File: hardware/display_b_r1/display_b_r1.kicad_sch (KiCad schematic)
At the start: 20 parts

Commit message: Display board layout is now 95% complete, the number of caps on the board might need some further tweaking and there are also some gaps where a few more LEDs could fit. Additionally I've decided to provide the option to use the hinges as the ground connection allowing more +5V channels on the FFC connectors which should mean more current carrying capacity. The new power board schematic has had some changes, namely the vreg has changed and so have some of the passives around it, more input protect has been added, a MOV for over voltage protection and an NMOS for reverse pol. Looking at the new vreg the power dissipation before it cooks itself (~1.1W) isn't great but it's enough for about 2.5A (at around 93% eff.) for the LEDs which hasn't usually been the bottleneck (looking at you 9V batteries). This means we're expecting around 1.8A peak input current at a Vin of 7V and need to size the fuze around that as much more current and the vreg is cooked. Might look into a over voltage shutout circuit if it seems like we're blowing fuses too often.
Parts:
- removed J?: 8-pin FPC Connector, symbol Connector_Generic:Conn_01x08
- added C109, C110, C111, C112, C113, C114, C115, C116, C117, C118, C119, C120, C121, C122, C123, C124, C125, C126, C127, C129, C130, C131, C132, C133, C134, C135, C136, C137, C138, C139, C140, C141, C142, C143, C144, C145, C146, C147: 22u 10V, Capacitor_SMD:C_0603_1608Metric, symbol Device:C_Small
- added D101, D102, D103, D104, D107, D108, D109, D110, D111, D112, D113, D114, D115, D116, D117, D118, D119, D120, D121, D122, D123, D124, D125, D126, D127, D128, D129, D130, D131, D132, D133, D134, D135, D136, D137, D138, D139, D140, D142, D143, D144, D145, D146, D147, D148, D149, D151, D152, D153, D154, D155, D156, D157, D158, D160, D161, D162, D163, D164, D165, D166, D167, D169, D170, D172, D173, D174, D175, D176, D178, D179, D180, D182, D183, D185, D188, D189, D191, D192, D193, D194, D196, D197, D199, D200, D202, D204, D205, D206, D207, D208, D209, D210, D212, D213, D214, D215, D216, D217, D218, D220, D221, D222, D223, D224, D225, D226, D229, D230, D231, D232, D233, D234, D235, D238, D239, D240, D241, D242, D243, D244, D247, D248, D249, D250, D251, D252, D253, D256, D257, D258, D259, D260, D261, D262, D265, D266, D267, D270, D271: APA102-2020, rave_shades:LED-APA102-2020, symbol LED:APA102-2020
- added H101, H102, H103, H104: MountingHole_Pad, rave_shades:M1.4 Mounting Hole, symbol Mechanical:MountingHole_Pad
- added J102: Conn_01x08, rave_shades:CF35082D0RE-NH, symbol rave_shades:Conn_01x08
- added JP101, JP102: SolderJumper_3_Open, Jumper:SolderJumper-3_P1.3mm_Open_Pad1.0x1.5mm, symbol Jumper:SolderJumper_3_Open
- C101, C102, C103, C104, C105, C106, C107, C108: renamed from C?; footprint (none) -> Capacitor_SMD:C_0603_1608Metric
- D187, D195, D203, D211, D219, D228, D237, D246, D255, D264: renamed from D?; footprint LED_SMD:LED-APA102-2020 -> rave_shades:LED-APA102-2020
- J101: renamed from J?; footprint (none) -> rave_shades:CF35082D0RE-NH; symbol Connector_Generic:Conn_01x08 -> rave_shades:Conn_01x08
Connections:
- net +5V: now also C109.1, C110.1, C111.1, C112.1, C113.1, C114.1, C115.1, C116.1, C117.1, C118.1, C119.1, C120.1, C121.1, C122.1, C123.1, C124.1, C125.1, C126.1, C127.1, C129.1, C130.1, C131.1, C132.1, C133.1, C134.1, C135.1, C136.1, C137.1, C138.1, C139.1, C140.1, C141.1, C142.1, C143.1, C144.1, C145.1, C146.1, C147.1, D101.1 (VDD), D102.1 (VDD), D103.1 (VDD), D104.1 (VDD), D107.1 (VDD), D108.1 (VDD), D109.1 (VDD), D110.1 (VDD), D111.1 (VDD), D112.1 (VDD), D113.1 (VDD), D114.1 (VDD), D115.1 (VDD), D116.1 (VDD), D117.1 (VDD), D118.1 (VDD), D119.1 (VDD), D120.1 (VDD), D121.1 (VDD), D122.1 (VDD), D123.1 (VDD), D124.1 (VDD), D125.1 (VDD), D126.1 (VDD), D127.1 (VDD), D128.1 (VDD), D129.1 (VDD), D130.1 (VDD), D131.1 (VDD), D132.1 (VDD), D133.1 (VDD), D134.1 (VDD), D135.1 (VDD), D136.1 (VDD), D137.1 (VDD), D138.1 (VDD), D139.1 (VDD), D140.1 (VDD), D142.1 (VDD), D143.1 (VDD), D144.1 (VDD), D145.1 (VDD), D146.1 (VDD), D147.1 (VDD), D148.1 (VDD), D149.1 (VDD), D151.1 (VDD), D152.1 (VDD), D153.1 (VDD), D154.1 (VDD), D155.1 (VDD), D156.1 (VDD), D157.1 (VDD), D158.1 (VDD), D160.1 (VDD), D161.1 (VDD), D162.1 (VDD), D163.1 (VDD), D164.1 (VDD), D165.1 (VDD), D166.1 (VDD), D167.1 (VDD), D169.1 (VDD), D170.1 (VDD), D172.1 (VDD), D173.1 (VDD), D174.1 (VDD), D175.1 (VDD), D176.1 (VDD), D178.1 (VDD), D179.1 (VDD), D180.1 (VDD), D182.1 (VDD), D183.1 (VDD), D185.1 (VDD), D188.1 (VDD), D189.1 (VDD), D191.1 (VDD), D192.1 (VDD), D193.1 (VDD), D194.1 (VDD), D196.1 (VDD), D197.1 (VDD), D199.1 (VDD), D200.1 (VDD), D202.1 (VDD), D204.1 (VDD), D205.1 (VDD), D206.1 (VDD), D207.1 (VDD), D208.1 (VDD), D209.1 (VDD), D210.1 (VDD), D212.1 (VDD), D213.1 (VDD), D214.1 (VDD), D215.1 (VDD), D216.1 (VDD), D217.1 (VDD), D218.1 (VDD), D220.1 (VDD), D221.1 (VDD), D222.1 (VDD), D223.1 (VDD), D224.1 (VDD), D225.1 (VDD), D226.1 (VDD), D229.1 (VDD), D230.1 (VDD), D231.1 (VDD), D232.1 (VDD), D233.1 (VDD), D234.1 (VDD), D235.1 (VDD), D238.1 (VDD), D239.1 (VDD), D240.1 (VDD), D241.1 (VDD), D242.1 (VDD), D243.1 (VDD), D244.1 (VDD), D247.1 (VDD), D248.1 (VDD), D249.1 (VDD), D250.1 (VDD), D251.1 (VDD), D252.1 (VDD), D253.1 (VDD), D256.1 (VDD), D257.1 (VDD), D258.1 (VDD), D259.1 (VDD), D260.1 (VDD), D261.1 (VDD), D262.1 (VDD), D265.1 (VDD), D266.1 (VDD), D267.1 (VDD), D270.1 (VDD), D271.1 (VDD), J102.4 (Pin_4), J102.5 (Pin_5), JP101.1 (A), JP102.1 (A)
- net GND: now also J101.9 (NC), C109.2, C110.2, C111.2, C112.2, C113.2, C114.2, C115.2, C116.2, C117.2, C118.2, C119.2, C120.2, C121.2, C122.2, C123.2, C124.2, C125.2, C126.2, C127.2, C129.2, C130.2, C131.2, C132.2, C133.2, C134.2, C135.2, C136.2, C137.2, C138.2, C139.2, C140.2, C141.2, C142.2, C143.2, C144.2, C145.2, C146.2, C147.2, D101.6 (GND), D102.6 (GND), D103.6 (GND), D104.6 (GND), D107.6 (GND), D108.6 (GND), D109.6 (GND), D110.6 (GND), D111.6 (GND), D112.6 (GND), D113.6 (GND), D114.6 (GND), D115.6 (GND), D116.6 (GND), D117.6 (GND), D118.6 (GND), D119.6 (GND), D120.6 (GND), D121.6 (GND), D122.6 (GND), D123.6 (GND), D124.6 (GND), D125.6 (GND), D126.6 (GND), D127.6 (GND), D128.6 (GND), D129.6 (GND), D130.6 (GND), D131.6 (GND), D132.6 (GND), D133.6 (GND), D134.6 (GND), D135.6 (GND), D136.6 (GND), D137.6 (GND), D138.6 (GND), D139.6 (GND), D140.6 (GND), D142.6 (GND), D143.6 (GND), D144.6 (GND), D145.6 (GND), D146.6 (GND), D147.6 (GND), D148.6 (GND), D149.6 (GND), D151.6 (GND), D152.6 (GND), D153.6 (GND), D154.6 (GND), D155.6 (GND), D156.6 (GND), D157.6 (GND), D158.6 (GND), D160.6 (GND), D161.6 (GND), D162.6 (GND), D163.6 (GND), D164.6 (GND), D165.6 (GND), D166.6 (GND), D167.6 (GND), D169.6 (GND), D170.6 (GND), D172.6 (GND), D173.6 (GND), D174.6 (GND), D175.6 (GND), D176.6 (GND), D178.6 (GND), D179.6 (GND), D180.6 (GND), D182.6 (GND), D183.6 (GND), D185.6 (GND), D188.6 (GND), D189.6 (GND), D191.6 (GND), D192.6 (GND), D193.6 (GND), D194.6 (GND), D196.6 (GND), D197.6 (GND), D199.6 (GND), D200.6 (GND), D202.6 (GND), D204.6 (GND), D205.6 (GND), D206.6 (GND), D207.6 (GND), D208.6 (GND), D209.6 (GND), D210.6 (GND), D212.6 (GND), D213.6 (GND), D214.6 (GND), D215.6 (GND), D216.6 (GND), D217.6 (GND), D218.6 (GND), D220.6 (GND), D221.6 (GND), D222.6 (GND), D223.6 (GND), D224.6 (GND), D225.6 (GND), D226.6 (GND), D229.6 (GND), D230.6 (GND), D231.6 (GND), D232.6 (GND), D233.6 (GND), D234.6 (GND), D235.6 (GND), D238.6 (GND), D239.6 (GND), D240.6 (GND), D241.6 (GND), D242.6 (GND), D243.6 (GND), D244.6 (GND), D247.6 (GND), D248.6 (GND), D249.6 (GND), D250.6 (GND), D251.6 (GND), D252.6 (GND), D253.6 (GND), D256.6 (GND), D257.6 (GND), D258.6 (GND), D259.6 (GND), D260.6 (GND), D261.6 (GND), D262.6 (GND), D265.6 (GND), D266.6 (GND), D267.6 (GND), D270.6 (GND), D271.6 (GND), H101.1, H102.1, H103.1, H104.1, J102.9 (NC), JP101.3 (B), JP102.3 (B); no longer J101.1 (Pin_1), J101.3 (Pin_3), J101.6 (Pin_6)
- net LED_CLK_5V0: now also J102.7 (Pin_7)
- net LED_MOSI_5V0: now also J102.8 (Pin_8)
- net SPARE_0_5V0: now also J102.2 (Pin_2)
- net SPARE_1_5V0: now also J102.1 (Pin_1)
- net at D187.2 (CKO): now also D188.5 (CKI)
- net at D187.3 (SDO): now also D188.4 (SDI)
- new net: D143.2 (CKO), D152.5 (CKI)
- new net: D143.3 (SDO), D152.4 (SDI)
- new net: D134.3 (SDO), D143.4 (SDI)
- new net: D134.2 (CKO), D143.5 (CKI)
- new net: D196.2 (CKO), D204.5 (CKI)
- new net: D196.3 (SDO), D204.4 (SDI)
- new net: D188.3 (SDO), D196.4 (SDI)
- new net: D188.2 (CKO), D196.5 (CKI)
- new net: D176.2 (CKO), D185.5 (CKI)
- new net: D176.3 (SDO), D185.4 (SDI)
- new net: D167.3 (SDO), D176.4 (SDI)
- new net: D167.2 (CKO), D176.5 (CKI)
- new net: D153.5 (CKI), D162.2 (CKO)
- new net: D153.4 (SDI), D162.3 (SDO)
- new net: D162.4 (SDI), D180.3 (SDO)
- new net: D162.5 (CKI), D180.2 (CKO)
- new net: D102.2 (CKO), D110.5 (CKI)
- new net: D102.3 (SDO), D110.4 (SDI)
- new net: D101.3 (SDO), D102.4 (SDI)
- new net: D101.2 (CKO), D102.5 (CKI)
- new net: D215.5 (CKI), D223.2 (CKO)
- new net: D215.4 (SDI), D223.3 (SDO)
- new net: D223.4 (SDI), D232.3 (SDO)
- new net: D223.5 (CKI), D232.2 (CKO)
- new net: D191.2 (CKO), D192.5 (CKI)
- new net: D191.3 (SDO), D192.4 (SDI)
- new net: D191.4 (SDI), D199.3 (SDO)
- new net: D191.5 (CKI), D199.2 (CKO)
- new net: D104.2 (CKO), D112.5 (CKI)
- new net: D104.3 (SDO), D112.4 (SDI)
- new net: D103.3 (SDO), D104.4 (SDI)
- new net: D103.2 (CKO), D104.5 (CKI)
- new net: D214.2 (CKO), D222.5 (CKI)
- new net: D214.3 (SDO), D222.4 (SDI)
- new net: D206.3 (SDO), D214.4 (SDI)
- new net: D206.2 (CKO), D214.5 (CKI)
- new net: D213.5 (CKI), D221.2 (CKO)
- new net: D213.4 (SDI), D221.3 (SDO)
- new net: D221.4 (SDI), D230.3 (SDO)
- new net: D221.5 (CKI), D230.2 (CKO)
- new net: D122.2 (CKO), D130.5 (CKI)
- new net: D122.3 (SDO), D130.4 (SDI)
- new net: D114.3 (SDO), D122.4 (SDI)
- new net: D114.2 (CKO), D122.5 (CKI)
- new net: D173.5 (CKI), D182.2 (CKO)
- new net: D173.4 (SDI), D182.3 (SDO)
- new net: D172.3 (SDO), D182.4 (SDI)
- new net: D172.2 (CKO), D182.5 (CKI)
- new net: D192.2 (CKO), D200.5 (CKI)
- new net: D192.3 (SDO), D200.4 (SDI)
- new net: D222.2 (CKO), D231.5 (CKI)
- new net: D222.3 (SDO), D231.4 (SDI)
- new net: D234.5 (CKI), D243.2 (CKO)
- new net: D234.4 (SDI), D243.3 (SDO)
- new net: D243.4 (SDI), D252.3 (SDO)
- new net: D243.5 (CKI), D252.2 (CKO)
- new net: D156.2 (CKO), D165.5 (CKI)
- new net: D156.3 (SDO), D165.4 (SDI)
- new net: D147.3 (SDO), D156.4 (SDI)
- new net: D147.2 (CKO), D156.5 (CKI)
- new net: D178.5 (CKI), D271.2 (CKO)
- new net: D178.4 (SDI), D271.3 (SDO)
- new net: D262.3 (SDO), D271.4 (SDI)
- new net: D262.2 (CKO), D271.5 (CKI)
- new net: D265.2 (CKO), D266.5 (CKI)
- new net: D265.3 (SDO), D266.4 (SDI)
- new net: D256.3 (SDO), D265.4 (SDI)
- new net: D256.2 (CKO), D265.5 (CKI)
- new net: D148.5 (CKI), D157.2 (CKO)
- new net: D148.4 (SDI), D157.3 (SDO)
- new net: D157.4 (SDI), D166.3 (SDO)
- new net: D157.5 (CKI), D166.2 (CKO)
- new net: D149.2 (CKO), D158.5 (CKI)
- new net: D149.3 (SDO), D158.4 (SDI)
- new net: D140.3 (SDO), D149.4 (SDI)
- new net: D140.2 (CKO), D149.5 (CKI)
- new net: D199.4 (SDI), D207.3 (SDO)
- new net: D199.5 (CKI), D207.2 (CKO)
- new net: D241.5 (CKI), D250.2 (CKO)
- new net: D241.4 (SDI), D250.3 (SDO)
- new net: D250.4 (SDI), D259.3 (SDO)
- new net: D250.5 (CKI), D259.2 (CKO)
- new net: D107.2 (CKO), D108.5 (CKI)
- new net: D107.3 (SDO), D108.4 (SDI)
- new net: D107.4 (SDI), D115.3 (SDO)
- new net: D107.5 (CKI), D115.2 (CKO)
- new net: D212.2 (CKO), D220.5 (CKI)
- new net: D212.3 (SDO), D220.4 (SDI)
- new net: D204.3 (SDO), D212.4 (SDI)
- new net: D204.2 (CKO), D212.5 (CKI)
- new net: D235.2 (CKO), D244.5 (CKI)
- new net: D235.3 (SDO), D244.4 (SDI)
- new net: D226.3 (SDO), D235.4 (SDI)
- new net: D226.2 (CKO), D235.5 (CKI)
- new net: D138.3 (SDO), D147.4 (SDI)
- new net: D138.2 (CKO), D147.5 (CKI)
- new net: D189.3 (SDO), D206.4 (SDI)
- new net: D189.2 (CKO), D206.5 (CKI)
- new net: D233.2 (CKO), D242.5 (CKI)
- new net: D233.3 (SDO), D242.4 (SDI)
- new net: D224.3 (SDO), D233.4 (SDI)
- new net: D224.2 (CKO), D233.5 (CKI)
- new net: D179.3 (SDO), D180.4 (SDI)
- new net: D179.2 (CKO), D180.5 (CKI)
- new net: D166.5 (CKI), D175.2 (CKO)
- new net: D166.4 (SDI), D175.3 (SDO)
- new net: D175.4 (SDI), D183.3 (SDO)
- new net: D175.5 (CKI), D183.2 (CKO)
- new net: D144.5 (CKI), D153.2 (CKO)
- new net: D144.4 (SDI), D153.3 (SDO)
- new net: D103.4 (SDI), D111.3 (SDO)
- new net: D103.5 (CKI), D111.2 (CKO)
- new net: D129.5 (CKI), D137.2 (CKO)
- new net: D129.4 (SDI), D137.3 (SDO)
- new net: D137.4 (SDI), D146.3 (SDO)
- new net: D137.5 (CKI), D146.2 (CKO)
- new net: D232.4 (SDI), D241.3 (SDO)
- new net: D232.5 (CKI), D241.2 (CKO)
- new net: D230.5 (CKI), D239.2 (CKO)
- new net: D230.4 (SDI), D239.3 (SDO)
- new net: D239.4 (SDI), D248.3 (SDO)
- new net: D239.5 (CKI), D248.2 (CKO)
- new net: D240.2 (CKO), D249.5 (CKI)
- new net: D240.3 (SDO), D249.4 (SDI)
- new net: D231.3 (SDO), D240.4 (SDI)
- new net: D231.2 (CKO), D240.5 (CKI)
- new net: D151.5 (CKI), D160.2 (CKO)
- new net: D151.4 (SDI), D160.3 (SDO)
- new net: D160.4 (SDI), D169.3 (SDO)
- new net: D160.5 (CKI), D169.2 (CKO)
- new net: D128.2 (CKO), D136.5 (CKI)
- new net: D128.3 (SDO), D136.4 (SDI)
- new net: D120.3 (SDO), D128.4 (SDI)
- new net: D120.2 (CKO), D128.5 (CKI)
- new net: D101.4 (SDI), D109.3 (SDO)
- new net: D101.5 (CKI), D109.2 (CKO)
- new net: D146.4 (SDI), D155.3 (SDO)
- new net: D146.5 (CKI), D155.2 (CKO)
- new net: D189.4 (SDI), D197.3 (SDO)
- new net: D189.5 (CKI), D197.2 (CKO)
- new net: D123.5 (CKI), D131.2 (CKO)
- new net: D123.4 (SDI), D131.3 (SDO)
- new net: D131.4 (SDI), D139.3 (SDO)
- new net: D131.5 (CKI), D139.2 (CKO)
- new net: D164.5 (CKI), D173.2 (CKO)
- new net: D164.4 (SDI), D173.3 (SDO)
- new net: D109.5 (CKI), D117.2 (CKO)
- new net: D109.4 (SDI), D117.3 (SDO)
- new net: D117.4 (SDI), D125.3 (SDO)
- new net: D117.5 (CKI), D125.2 (CKO)
- new net: D112.3 (SDO), D120.4 (SDI)
- new net: D112.2 (CKO), D120.5 (CKI)
- new net: D125.4 (SDI), D133.3 (SDO)
- new net: D125.5 (CKI), D133.2 (CKO)
- new net: D113.2 (CKO), D114.5 (CKI)
- new net: D113.3 (SDO), D114.4 (SDI)
- new net: D113.4 (SDI), D121.3 (SDO)
- new net: D113.5 (CKI), D121.2 (CKO)
- new net: D110.2 (CKO), D118.5 (CKI)
- new net: D110.3 (SDO), D118.4 (SDI)
- new net: D197.4 (SDI), D205.3 (SDO)
- new net: D197.5 (CKI), D205.2 (CKO)
- new net: D126.2 (CKO), D134.5 (CKI)
- new net: D126.3 (SDO), D134.4 (SDI)
- new net: D118.3 (SDO), D126.4 (SDI)
- new net: D118.2 (CKO), D126.5 (CKI)
- new net: D163.3 (SDO), D172.4 (SDI)
- new net: D163.2 (CKO), D172.5 (CKI)
- new net: D249.2 (CKO), D258.5 (CKI)
- new net: D249.3 (SDO), D258.4 (SDI)
- new net: D260.2 (CKO), D270.5 (CKI)
- new net: D260.3 (SDO), D270.4 (SDI)
- new net: D251.3 (SDO), D260.4 (SDI)
- new net: D251.2 (CKO), D260.5 (CKI)
- new net: D257.5 (CKI), D266.2 (CKO)
- new net: D257.4 (SDI), D266.3 (SDO)
- new net: D136.2 (CKO), D145.5 (CKI)
- new net: D136.3 (SDO), D145.4 (SDI)
- new net: D205.4 (SDI), D213.3 (SDO)
- new net: D205.5 (CKI), D213.2 (CKO)
- new net: D244.2 (CKO), D253.5 (CKI)
- new net: D244.3 (SDO), D253.4 (SDI)
- new net: D217.5 (CKI), D225.2 (CKO)
- new net: D217.4 (SDI), D225.3 (SDO)
- new net: D225.4 (SDI), D234.3 (SDO)
- new net: D225.5 (CKI), D234.2 (CKO)
- new net: D108.2 (CKO), D116.5 (CKI)
- new net: D108.3 (SDO), D116.4 (SDI)
- new net: D127.5 (CKI), D135.2 (CKO)
- new net: D127.4 (SDI), D135.3 (SDO)
- new net: D135.4 (SDI), D144.3 (SDO)
- new net: D135.5 (CKI), D144.2 (CKO)
- new net: D259.4 (SDI), D267.3 (SDO)
- new net: D259.5 (CKI), D267.2 (CKO)
- new net: D247.3 (SDO), D256.4 (SDI)
- new net: D247.2 (CKO), D256.5 (CKI)
- new net: D258.3 (SDO), D267.4 (SDI)
- new net: D258.2 (CKO), D267.5 (CKI)
- new net: D252.5 (CKI), D261.2 (CKO)
- new net: D252.4 (SDI), D261.3 (SDO)
- new net: D261.4 (SDI), D270.3 (SDO)
- new net: D261.5 (CKI), D270.2 (CKO)
- new net: D116.2 (CKO), D124.5 (CKI)
- new net: D116.3 (SDO), D124.4 (SDI)
- new net: D170.3 (SDO), D179.4 (SDI)
- new net: D170.2 (CKO), D179.5 (CKI)
- new net: D218.3 (SDO), D226.4 (SDI)
- new net: D218.2 (CKO), D226.5 (CKI)
- new net: D242.3 (SDO), D251.4 (SDI)
- new net: D242.2 (CKO), D251.5 (CKI)
- new net: D207.4 (SDI), D215.3 (SDO)
- new net: D207.5 (CKI), D215.2 (CKO)
- new net: D253.3 (SDO), D262.4 (SDI)
- new net: D253.2 (CKO), D262.5 (CKI)
- new net: D152.2 (CKO), D161.5 (CKI)
- new net: D152.3 (SDO), D161.4 (SDI)
- new net: D155.4 (SDI), D164.3 (SDO)
- new net: D155.5 (CKI), D164.2 (CKO)
- new net: D202.2 (CKO), D210.5 (CKI)
- new net: D202.3 (SDO), D210.4 (SDI)
- new net: D194.3 (SDO), D202.4 (SDI)
- new net: D194.2 (CKO), D202.5 (CKI)
- new net: D248.5 (CKI), D257.2 (CKO)
- new net: D248.4 (SDI), D257.3 (SDO)
- new net: D145.2 (CKO), D154.5 (CKI)
- new net: D145.3 (SDO), D154.4 (SDI)
- new net: D165.2 (CKO), D174.5 (CKI)
- new net: D165.3 (SDO), D174.4 (SDI)
- new net: D193.5 (CKI), D209.2 (CKO)
- new net: D193.4 (SDI), D209.3 (SDO)
- new net: D209.4 (SDI), D217.3 (SDO)
- new net: D209.5 (CKI), D217.2 (CKO)
- new net: D133.5 (CKI), D142.2 (CKO)
- new net: D133.4 (SDI), D142.3 (SDO)
- new net: D142.4 (SDI), D151.3 (SDO)
- new net: D142.5 (CKI), D151.2 (CKO)
- new net: D210.2 (CKO), D218.5 (CKI)
- new net: D210.3 (SDO), D218.4 (SDI)
- new net: D174.2 (CKO), D183.5 (CKI)
- new net: D174.3 (SDO), D183.4 (SDI)
- new net: D111.4 (SDI), D119.3 (SDO)
- new net: D111.5 (CKI), D119.2 (CKO)
- new net: D208.2 (CKO), D216.5 (CKI)
- new net: D208.3 (SDO), D216.4 (SDI)
- new net: D200.3 (SDO), D208.4 (SDI)
- new net: D200.2 (CKO), D208.5 (CKI)
- new net: D216.2 (CKO), D224.5 (CKI)
- new net: D216.3 (SDO), D224.4 (SDI)
- new net: D229.2 (CKO), D238.5 (CKI)
- new net: D229.3 (SDO), D238.4 (SDI)
- new net: D220.3 (SDO), D229.4 (SDI)
- new net: D220.2 (CKO), D229.5 (CKI)
- new net: D119.4 (SDI), D127.3 (SDO)
- new net: D119.5 (CKI), D127.2 (CKO)
- new net: D139.4 (SDI), D148.3 (SDO)
- new net: D139.5 (CKI), D148.2 (CKO)
- new net: D169.5 (CKI), D178.2 (CKO)
- new net: D169.4 (SDI), D178.3 (SDO)
- new net: D238.3 (SDO), D247.4 (SDI)
- new net: D238.2 (CKO), D247.5 (CKI)
- new net: D124.2 (CKO), D132.5 (CKI)
- new net: D124.3 (SDO), D132.4 (SDI)
- new net: D158.3 (SDO), D167.4 (SDI)
- new net: D158.2 (CKO), D167.5 (CKI)
- new net: D121.4 (SDI), D129.3 (SDO)
- new net: D121.5 (CKI), D129.2 (CKO)
- new net: D154.3 (SDO), D163.4 (SDI)
- new net: D154.2 (CKO), D163.5 (CKI)
- new net: D161.3 (SDO), D170.4 (SDI)
- new net: D161.2 (CKO), D170.5 (CKI)
- new net: D132.3 (SDO), D140.4 (SDI)
- new net: D132.2 (CKO), D140.5 (CKI)
- new net: D115.5 (CKI), D123.2 (CKO)
- new net: D115.4 (SDI), D123.3 (SDO)
- new net: D193.2 (CKO), D194.5 (CKI)
- new net: D193.3 (SDO), D194.4 (SDI)
- new net: D130.3 (SDO), D138.4 (SDI)
- new net: D130.2 (CKO), D138.5 (CKI)
- new net 5V0_OR_GND_1: J101.1 (Pin_1), J101.3 (Pin_3), J101.6 (Pin_6), JP101.2 (C)
- new net 5V0_OR_GND_2: J102.3 (Pin_3), J102.6 (Pin_6), JP102.2 (C)
- no-connect marks 0 -> 2
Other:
- note added: "Use these solder jumpers to chose between using the cable to carry the return current or rely soley on the hinges. Might be needed to provide sufficient current but the hinges could prove unreliable connectors."
- moved on the sheet: C101, C102, C103, C104, C105, C106, C107, C108

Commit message: Next revision of the boards are finished and ready for fabrication, and a BOM has been added.
The BOM is still missing components for the nucleo shield.
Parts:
- added C128, C148, C149, C150, C151, C152, C153, C154, C155, C156, C157, C158, C159, C160, C161, C162, C163, C164, C165, C166, C167, C168, C169, C170, C171, C172, C173, C174, C175, C176, C177, C178, C179, C180, C181, C182, C183, C184, C185, C186, C187, C188, C189, C190, C191, C192, C193, C194, C195, C196, C197, C198, C199, C200, C201, C202, C203, C204, C205, C206, C207, C208, C209, C210, C211, C212, C213, C214, C215, C216, C217, C218, C219, C220, C221, C222, C223, C224, C225, C226, C227, C228, C229, C230, C231, C232: 1u, rave_shades:0603_1608, symbol Device:C_Small
- C101, C102, C103, C104, C105, C106, C107, C108, C109, C110, C111, C112, C113, C114, C115, C116, C117, C118, C119, C120, C121, C122, C123, C124, C125, C126, C127, C129, C130, C131, C132, C133, C134, C135, C136, C137, C138, C139, C140, C141, C142, C143, C144, C145, C146, C147: value 22u 10V -> 1u; footprint Capacitor_SMD:C_0603_1608Metric -> rave_shades:0603_1608; Item Link https://www.digikey.com.au/en/products/detail/murata-electr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 -> https://www.digikey.com.au/en/products/detail/samsung-elect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
- D101, D102, D103, D104, D107, D108, D109, D110, D111, D112, D113, D114, D115, D116, D117, D118, D119, D120, D121, D122, D123, D124, D125, D126, D127, D128, D129, D130, D131, D132, D133, D134, D135, D136, D137, D138, D139, D140, D142, D143, D144, D145, D146, D147, D148, D149, D151, D152, D153, D154, D155, D156, D157, D158, D160, D161, D162, D163, D164, D165, D166, D167, D169, D170, D172, D173, D174, D175, D176, D178, D179, D180, D182, D183, D185, D187, D188, D189, D191, D192, D193, D194, D195, D196, D197, D199, D200, D202, D203, D204, D205, D206, D207, D208, D209, D210, D211, D212, D213, D214, D215, D216, D217, D218, D219, D220, D221, D222, D223, D224, D225, D226, D228, D229, D230, D231, D232, D233, D234, D235, D237, D238, D239, D240, D241, D242, D243, D244, D246, D247, D248, D249, D250, D251, D252, D253, D255, D256, D257, D258, D259, D260, D261, D262, D264, D265, D266, D267, D270, D271: Item Link (none) -> https://www.aliexpress.com/item/10000013471219.html
- H101, H102, H103, H104: now left out of the parts list
- J101, J102: Item Link (none) -> https://www.digikey.com.au/en/products/detail/cvilux-usa/CF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
- JP101, JP102: footprint Jumper:SolderJumper-3_P1.3mm_Open_Pad1.0x1.5mm -> rave_shades:SolderJumper-3_P1.3mm_Open_Pad1.0x1.5mm; now left out of the parts list
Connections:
- net +5V: now also C102.2, C104.2, C106.2, C108.2, C110.2, C112.2, C114.2, C116.2, C117.2, C119.2, C130.2, C133.2, C135.2, C137.2, C139.2, C141.2, C143.2, C144.2, C145.2, C147.2, C128.1, C148.1, C149.1, C150.1, C151.1, C152.1, C153.1, C154.1, C155.1, C156.1, C157.2, C158.2, C159.2, C160.2, C161.2, C162.2, C163.2, C164.2, C165.2, C166.2, C167.1, C168.1, C169.1, C170.1, C171.1, C172.1, C173.1, C174.1, C175.1, C176.1, C177.2, C178.2, C179.2, C180.2, C181.2, C182.2, C183.2, C184.2, C185.2, C186.2, C187.1, C188.1, C189.1, C190.1, C191.1, C192.1, C193.1, C194.1, C195.1, C196.1, C197.2, C198.2, C199.2, C200.2, C201.2, C202.2, C203.2, C204.2, C205.2, C206.2, C207.1, C208.1, C209.1, C210.1, C211.1, C212.1, C213.1, C214.1, C215.1, C216.1, C217.2, C218.2, C219.2, C220.2, C221.2, C222.2, C223.2, C224.2, C225.2, C226.2, C227.1, C228.1, C229.1, C230.1, C231.2, C232.2; no longer C102.1, C104.1, C106.1, C108.1, C110.1, C112.1, C114.1, C116.1, C117.1, C119.1, C130.1, C133.1, C135.1, C137.1, C139.1, C141.1, C143.1, C144.1, C145.1, C147.1
- net GND: now also C102.1, C104.1, C106.1, C108.1, C110.1, C112.1, C114.1, C116.1, C117.1, C119.1, C130.1, C133.1, C135.1, C137.1, C139.1, C141.1, C143.1, C144.1, C145.1, C147.1, C128.2, C148.2, C149.2, C150.2, C151.2, C152.2, C153.2, C154.2, C155.2, C156.2, C157.1, C158.1, C159.1, C160.1, C161.1, C162.1, C163.1, C164.1, C165.1, C166.1, C167.2, C168.2, C169.2, C170.2, C171.2, C172.2, C173.2, C174.2, C175.2, C176.2, C177.1, C178.1, C179.1, C180.1, C181.1, C182.1, C183.1, C184.1, C185.1, C186.1, C187.2, C188.2, C189.2, C190.2, C191.2, C192.2, C193.2, C194.2, C195.2, C196.2, C197.1, C198.1, C199.1, C200.1, C201.1, C202.1, C203.1, C204.1, C205.1, C206.1, C207.2, C208.2, C209.2, C210.2, C211.2, C212.2, C213.2, C214.2, C215.2, C216.2, C217.1, C218.1, C219.1, C220.1, C221.1, C222.1, C223.1, C224.1, C225.1, C226.1, C227.2, C228.2, C229.2, C230.2, C231.1, C232.1; no longer C102.2, C104.2, C106.2, C108.2, C110.2, C112.2, C114.2, C116.2, C117.2, C119.2, C130.2, C133.2, C135.2, C137.2, C139.2, C141.2, C143.2, C144.2, C145.2, C147.2, J101.9 (NC), J102.9 (NC)
- no-connect marks 2 -> 4
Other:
- moved on the sheet: C101, C102, C103, C104, C105, C106, C107, C108, C109, C110, C111, C112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

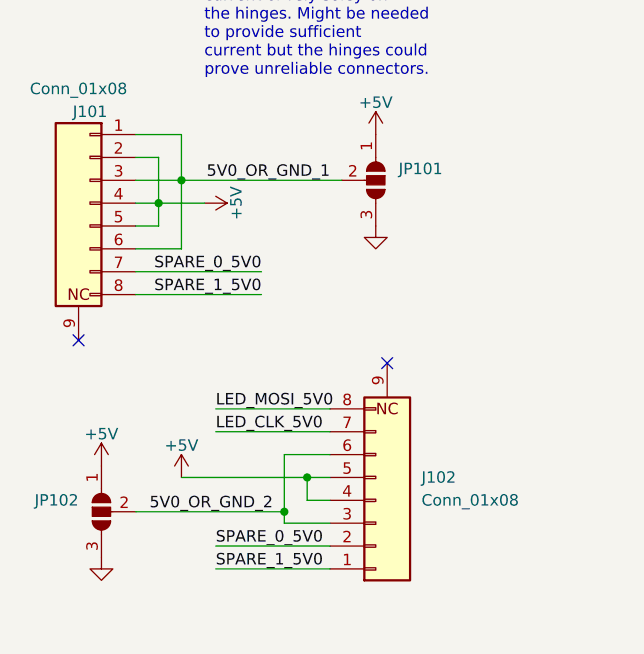
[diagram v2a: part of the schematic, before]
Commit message: Updated kicad files to work with latest kicad. Added some todos for next hw design.
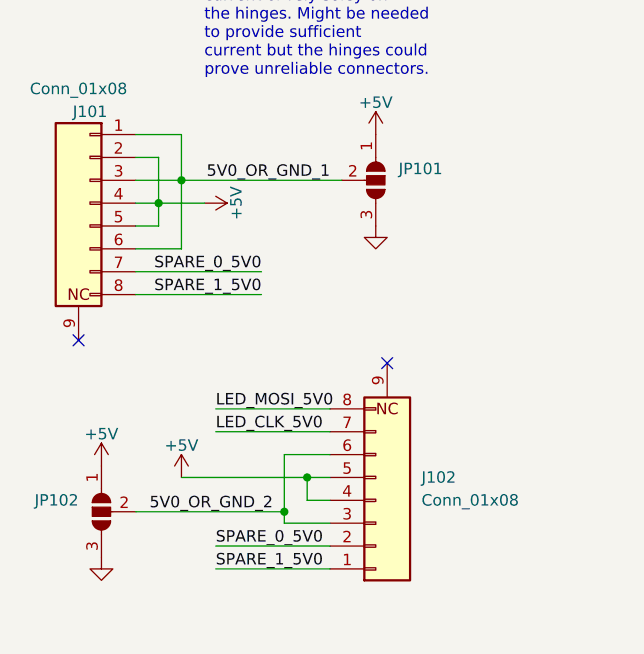
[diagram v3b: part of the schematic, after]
